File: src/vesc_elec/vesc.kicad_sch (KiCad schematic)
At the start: 23 parts, among them J1 Conn_01x02, J2 Conn_01x03, J3 Conn_01x02, P4 HALL/Encoder

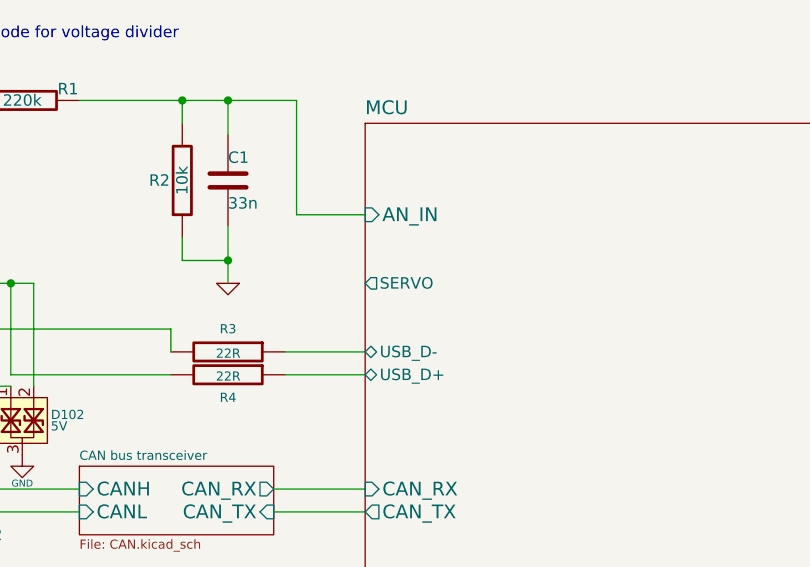
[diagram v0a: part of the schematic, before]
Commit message: Remove extra footprint libraries
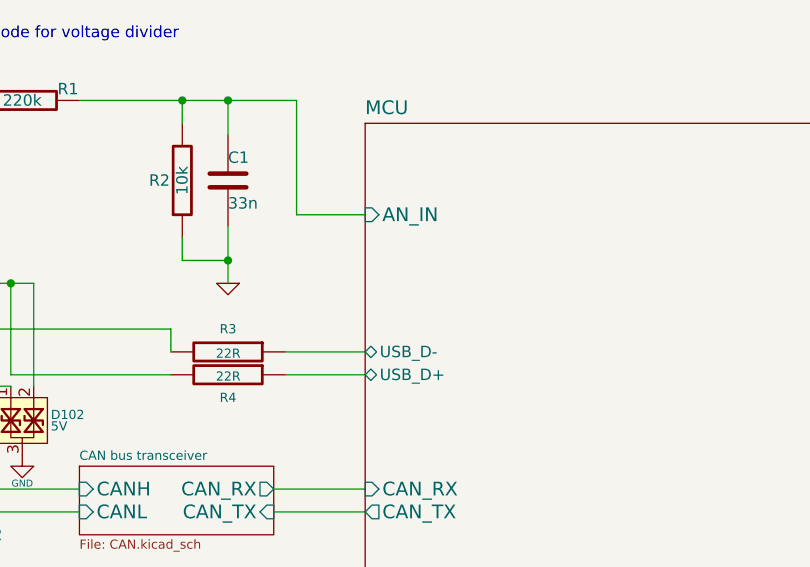
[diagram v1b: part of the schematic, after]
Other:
- sheet MCU ports: added none; removed SERVO
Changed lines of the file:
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@@
-			)
-		)
-		(pin "SERVO" output
-			(at 161.29 113.03 180)
-			(effects
-				(font
-					(size 1.27 1.27)
-				)
-				(justify left)
 			)
 		)

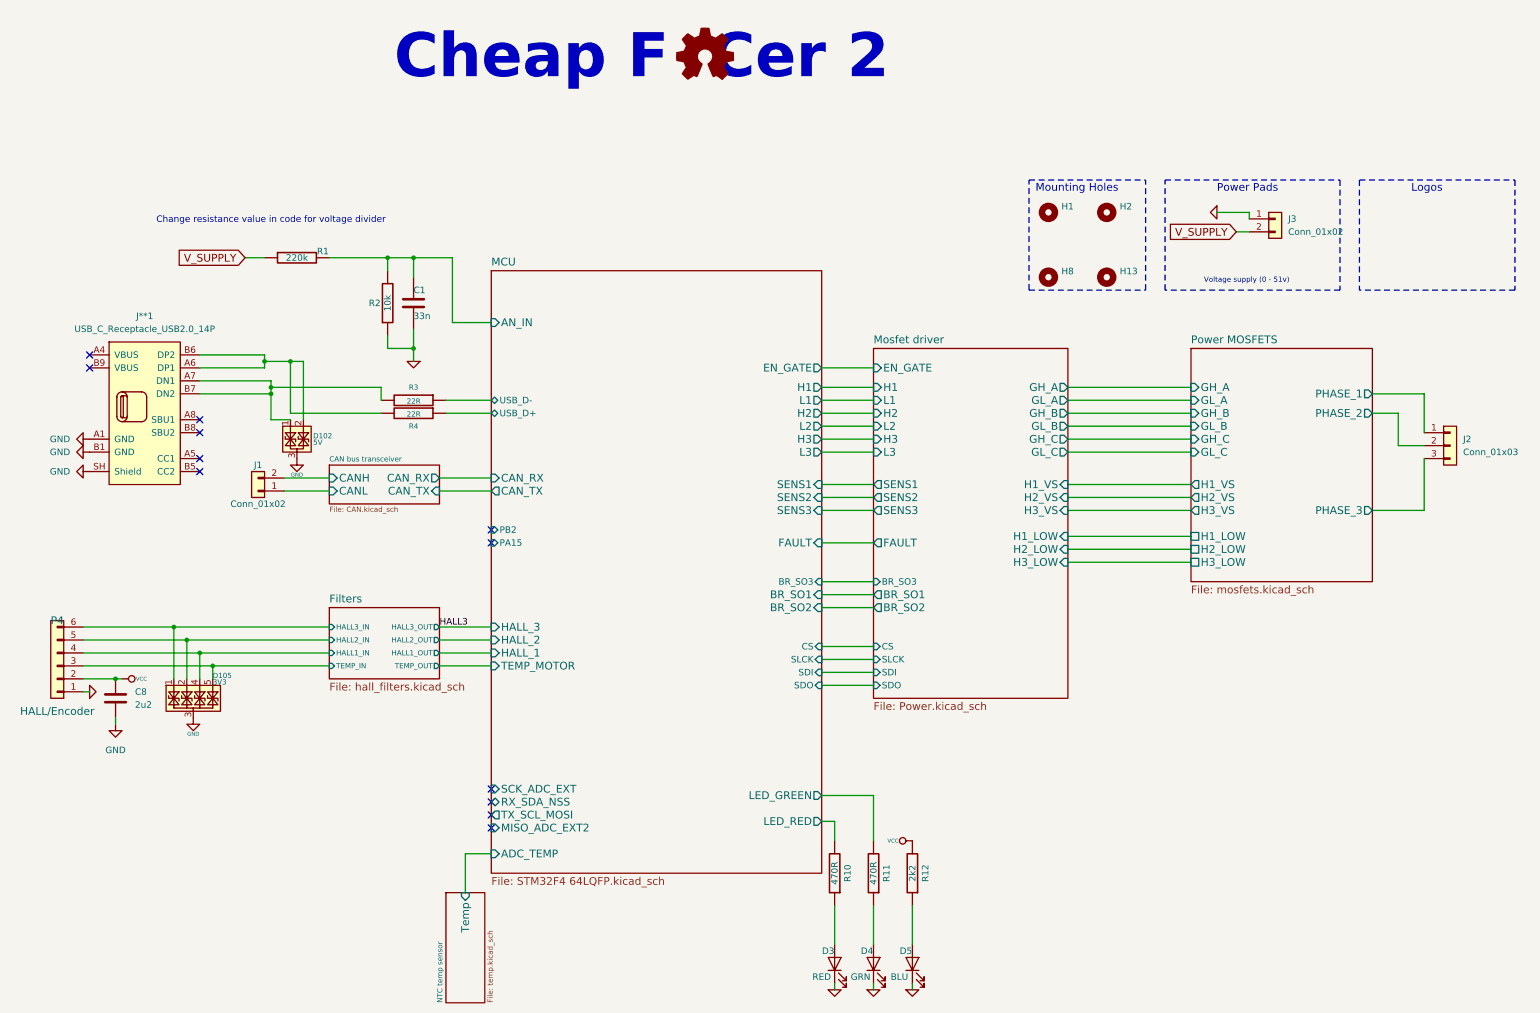
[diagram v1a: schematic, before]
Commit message: Remove unused pins on VESC schematic
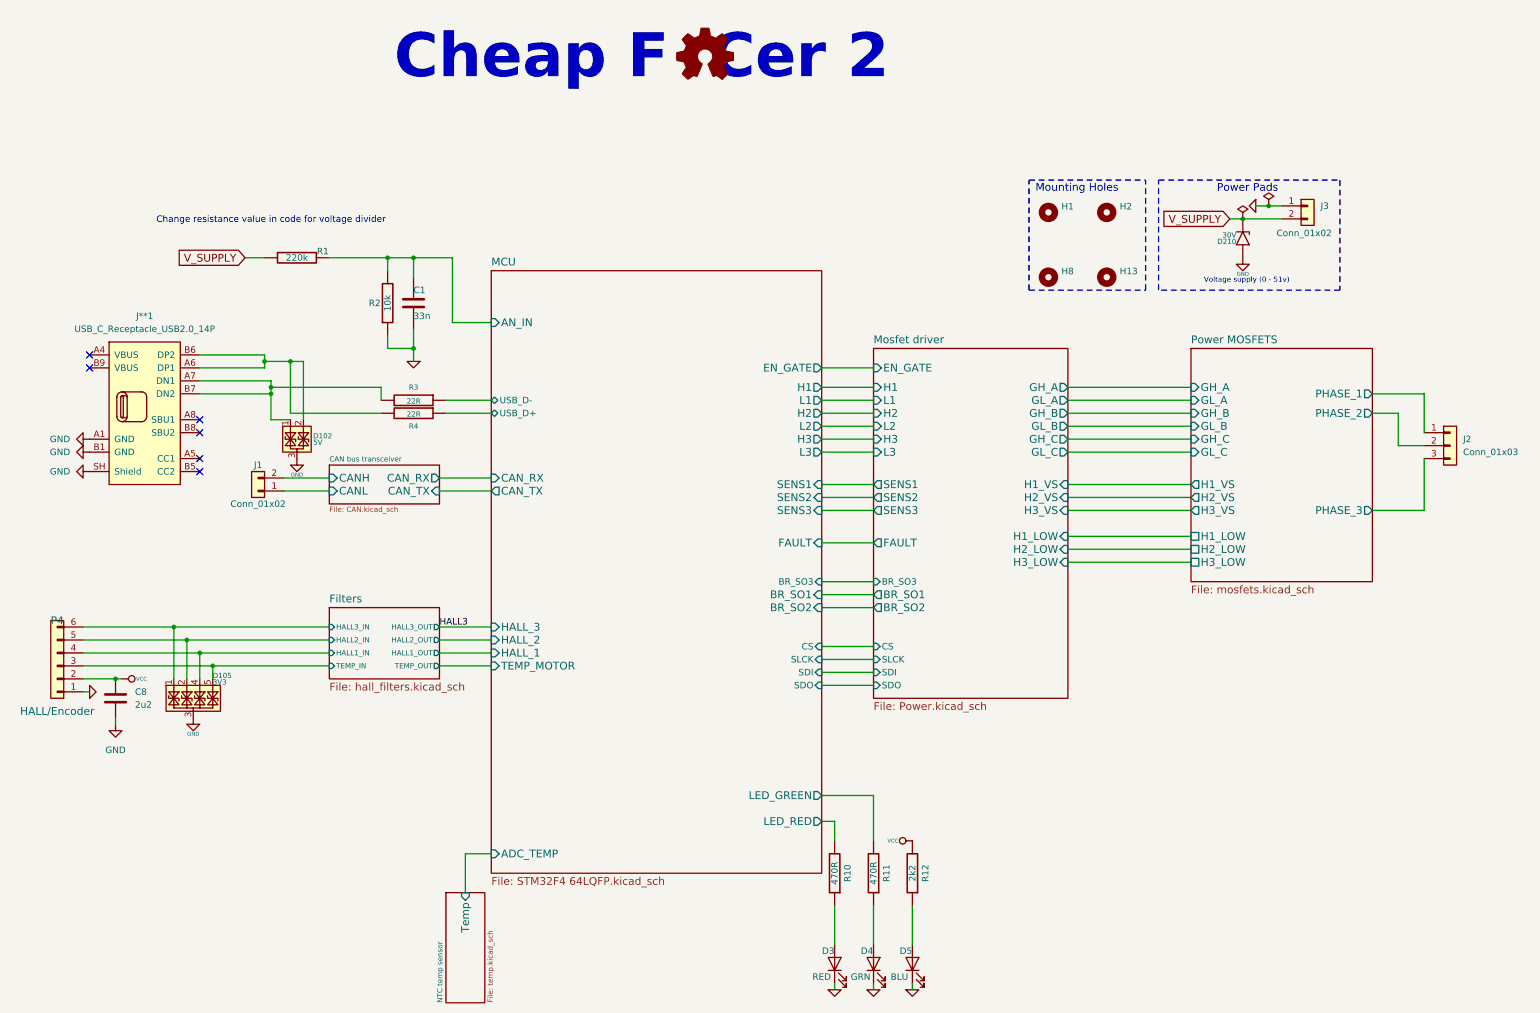
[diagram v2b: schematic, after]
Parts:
- added D210: 30V, Diode_SMD:D_SMF, symbol Diode:SMF30A
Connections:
- net GND: now also D210.2 (A2)
- net V_SUPPLY: now also D210.1 (A1)
- no-connect marks 12 -> 6
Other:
- sheet MCU ports: added none; removed MISO_ADC_EXT2, PA15, PB2, RX_SDA_NSS, SCK_ADC_EXT, TX_SCL_MOSI
- note removed: "Logos"
- moved on the sheet: J3
